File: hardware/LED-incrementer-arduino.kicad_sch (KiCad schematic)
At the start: 3 parts, among them SW1 SW_Push, SW2 SW_Push

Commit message: Rev A 10029482-3 Schematic
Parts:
- removed SW2: SW_Push, symbol Switch:SW_Push
- added D1: LED_RED, symbol Device:LED
- added D2: LED_BLUE, symbol Device:LED
- added R1, R2: 470, symbol Device:R_US
- SW1: value SW_Push -> SW_Push_Button
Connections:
- net INCREMENT_BUTTON: now reaches SW1.1
- net INCREMENT_BUTTON: now also A1.D2
- net GND: now reaches SW1.2
- net GND: now also A1.GND1 (GND), D1.1 (K), D2.1 (K)
- net BLINKER_LED: now reaches A1.D13
- net BLINKER_LED: now also R1.1
- net STATUS_LED: now reaches A1.D4
- net STATUS_LED: now also R2.1
- new net: D1.2 (A), R1.2
- new net: D2.2 (A), R2.2
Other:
- note added: "NOTES: 1. INT_INCR uses internal MCU pull-up. Active LOW. 2. POWER INPUT: USB-C 5 V via Arduino Uno R4 WiFi onboard connector."
- moved on the sheet: SW1

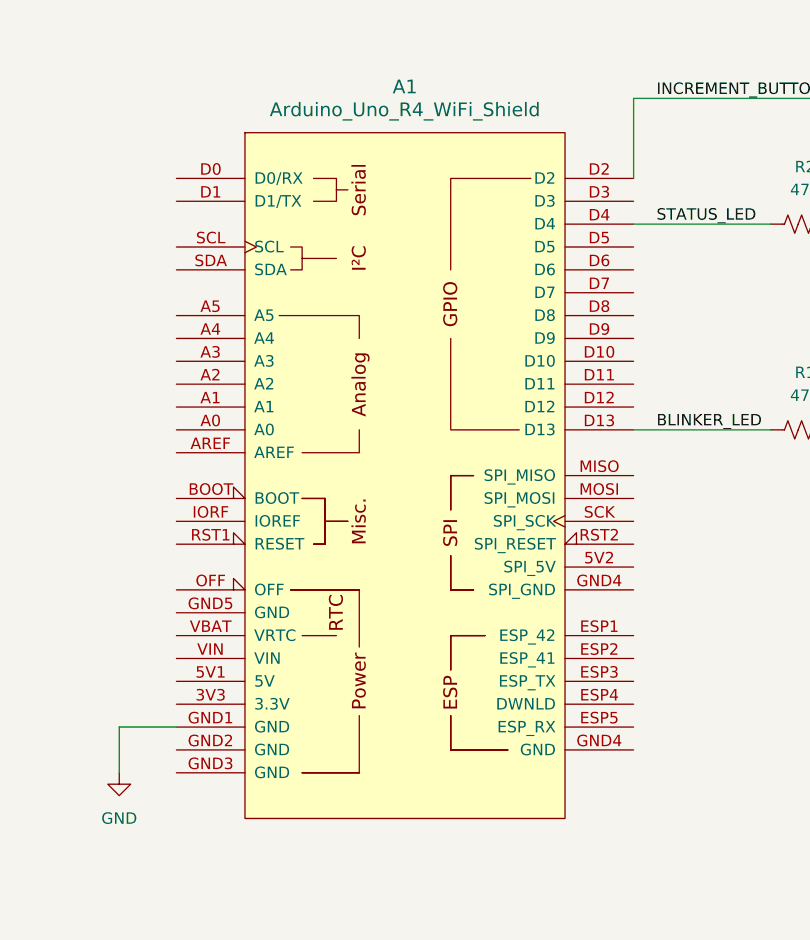
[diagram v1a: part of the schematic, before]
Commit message: Add assembly documentation and test plan for LED Incrementer Arduino
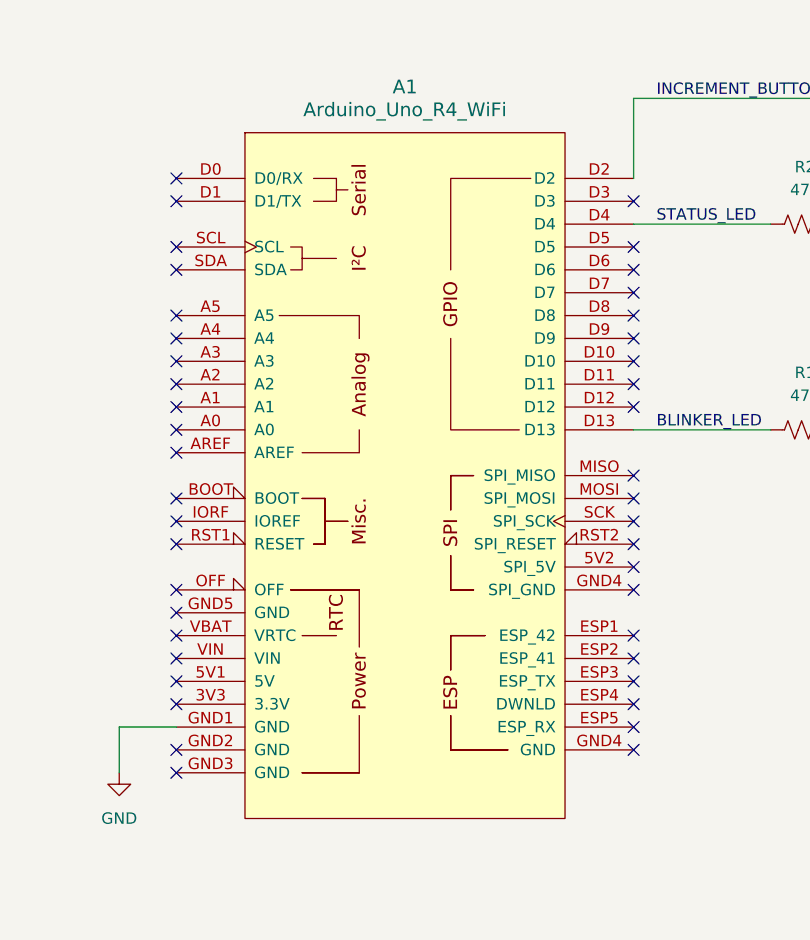
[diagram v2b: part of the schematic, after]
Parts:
- A1: value Arduino_Uno_R4_WiFi_Shield -> Arduino_Uno_R4_WiFi; MPN (none) -> ABX00087
- SW1: MPN (none) -> B3F-1000
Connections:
- no-connect marks 0 -> 43
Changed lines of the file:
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@@
 		(color 0 0 0 0)
+	)
+	(no_connect
+		(at 114.3 83.82)
+	)
+	(no_connect
+		(at 114.3 76.2)
+	)
+	(no_connect
+		(at 114.3 60.96)
+	)
+	(no_connect
+		(at 165.1 111.76)
+	)
+	(no_connect
+		(at 114.3 99.06)
+	)
+	(no_connect
+		(at 114.3 116.84)
+	)
+	(no_connect
+		(at 114.3 88.9)
+	)
+	(no_connect
+		(at 165.1 93.98)
+	)
+	(no_connect
+		(at 165.1 99.06)
+	)
+	(no_connect
+		(at 165.1 55.88)
+	)
+	(no_connect
+		(at 114.3 104.14)
+	)
+	(no_connect
+		(at 165.1 78.74)
+	)
+	(no_connect
+		(at 114.3 106.68)
+	)
+	(no_connect
+		(at 114.3 73.66)
+	)
+	(no_connect
+		(at 165.1 116.84)
+	)
+	(no_connect
+		(at 114.3 63.5)
+	)
+	(no_connect
+		(at 114.3 111.76)
+	)
+	(no_connect
+		(at 165.1 66.04)
+	)
+	(no_connect
+		(at 114.3 71.12)
+	)
+	(no_connect
+		(at 165.1 88.9)
+	)
+	(no_connect
+		(at 165.1 76.2)
+	)
+	(no_connect
+		(at 165.1 104.14)
+	)
+	(no_connect
+		(at 114.3 93.98)
+	)
+	(no_connect
+		(at 114.3 91.44)
+	)
+	(no_connect
+		(at 165.1 71.12)
+	)
+	(no_connect
+		(at 165.1 60.96)
+	)
+	(no_connect
+		(at 165.1 86.36)
+	)
+	(no_connect
+		(at 114.3 119.38)
+	)
+	(no_connect
+		(at 165.1 114.3)
+	)
+	(no_connect
+		(at 165.1 109.22)
+	)
+	(no_connect
+		(at 114.3 109.22)
+	)
+	(no_connect
+		(at 114.3 78.74)
+	)
+	(no_connect
+		(at 165.1 106.68)
+	)
+	(no_connect
+		(at 114.3 68.58)
+	)
+	(no_connect
+		(at 114.3 81.28)
+	)
+	(no_connect
+		(at 165.1 63.5)
+	)
+	(no_connect
+		(at 165.1 73.66)
+	)
+	(no_connect
+		(at 165.1 96.52)
+	)
+	(no_connect
+		(at 114.3 101.6)
+	)
+	(no_connect
+		(at 114.3 53.34)
+	)
+	(no_connect
+		(at 165.1 68.58)
+	)
+	(no_connect
+		(at 165.1 91.44)
+	)
+	(no_connect
+		(at 114.3 55.88)
 	)
 	(wire
@@
 			)
 		)
-		(property "Description" "Resistor, US symbol"
+		(property "Description" "Resistor, US symbol, 1/4 W, 5% Tol"
 			(at 184.15 81.28 0)
+			(hide yes)
+			(show_name no)
+			(do_not_autoplace no)
+			(effects
+				(font
+					(size 1.27 1.27)
+				)
+			)
+		)
+		(property "MPN" ""
+			(at 184.15 81.28 90)
 			(hide yes)
 			(show_name no)
@@
 			)
 		)
-		(property "Datasheet" ""
+		(property "Datasheet" "https://omronfs.omron.com/en_US/ecb/products/pdf/en-b3f.pdf"
 			(at 194.31 39.37 0)
 			(hide yes)
@@
 		)
 		(property "Description" "Push button switch, generic, two pins"
+			(at 194.31 44.45 0)
+			(hide yes)
+			(show_name no)
+			(do_not_autoplace no)
+			(effects
+				(font
+					(size 1.27 1.27)
+				)
+			)
+		)
+		(property "MPN" "B3F-1000"
 			(at 194.31 44.45 0)
 			(hide yes)
@@
 			)
 		)
-		(property "Description" "Resistor, US symbol"
+		(property "Description" "Resistor, US symbol, 1/4 W, 5% Tol"
 			(at 184.15 58.42 0)
+			(hide yes)
+			(show_name no)
+			(do_not_autoplace no)
+			(effects
+				(font
+					(size 1.27 1.27)
+				)
+			)
+		)
+		(property "MPN" ""
+			(at 184.15 58.42 90)
 			(hide yes)
 			(show_name no)
@@
 			)
 		)
-		(property "Description" "Light emitting diode"
+		(property "Description" "Light emitting diode, Generic 3mm, Red"
 			(at 199.39 81.28 0)
 			(hide yes)
@@
 		)
 		(property "Sim.Pins" "1=K 2=A"
+			(at 199.39 81.28 0)
+			(hide yes)
+			(show_name no)
+			(do_not_autoplace no)
+			(effects
+				(font
+					(size 1.27 1.27)
+				)
+			)
+		)
+		(property "MPN" ""
 			(at 199.39 81.28 0)
 			(hide yes)
@@
 			)
 		)
-		(property "Description" "Light emitting diode"
+		(property "Description" "Light emitting diode, , Generic 3mm, Blue"
 			(at 199.39 58.42 0)
 			(hide yes)
@@
 		)
 		(property "Sim.Pins" "1=K 2=A"
+			(at 199.39 58.42 0)
+			(hide yes)
+			(show_name no)
+			(do_not_autoplace no)
+			(effects
+				(font
+					(size 1.27 1.27)
+				)
+			)
+		)
+		(property "MPN" ""
 			(at 199.39 58.42 0)
 			(hide yes)
@@
 			)
 		)
-		(property "Value" "Arduino_Uno_R4_WiFi_Shield"
+		(property "Value" "Arduino_Uno_R4_WiFi"
 			(at 139.7 45.72 0)
 			(show_name no)
@@
 			)
 		)
-		(property "Description" "Shield for Arduino Uno R4 WiFi"
+		(property "Description" "Arduino Uno R4 WiFi"
 			(at 139.7 86.36 0)
 			(hide yes)
+			(show_name no)
+			(do_not_autoplace no)
+			(effects
+				(font
+					(size 1.27 1.27)
+				)
+			)
+		)
+		(property "MPN" "ABX00087"
+			(at 139.7 86.36 0)
+			(hide yes)
